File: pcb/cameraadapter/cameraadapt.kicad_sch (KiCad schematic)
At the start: 53 parts, among them J1 Conn_01x30_MountingPin, J2 Conn_01x24_MountingPin, J3 Conn_02x15_Odd_Even_MountingP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, J4 Conn_02x15_Odd_Even_MountingP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, J5 Conn_01x22_MountingPin, J6 Conn_01x22_MountingPin, Q1 DMG1024UV, U1 AP3429K, U3 ADP123, U4 ADP123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

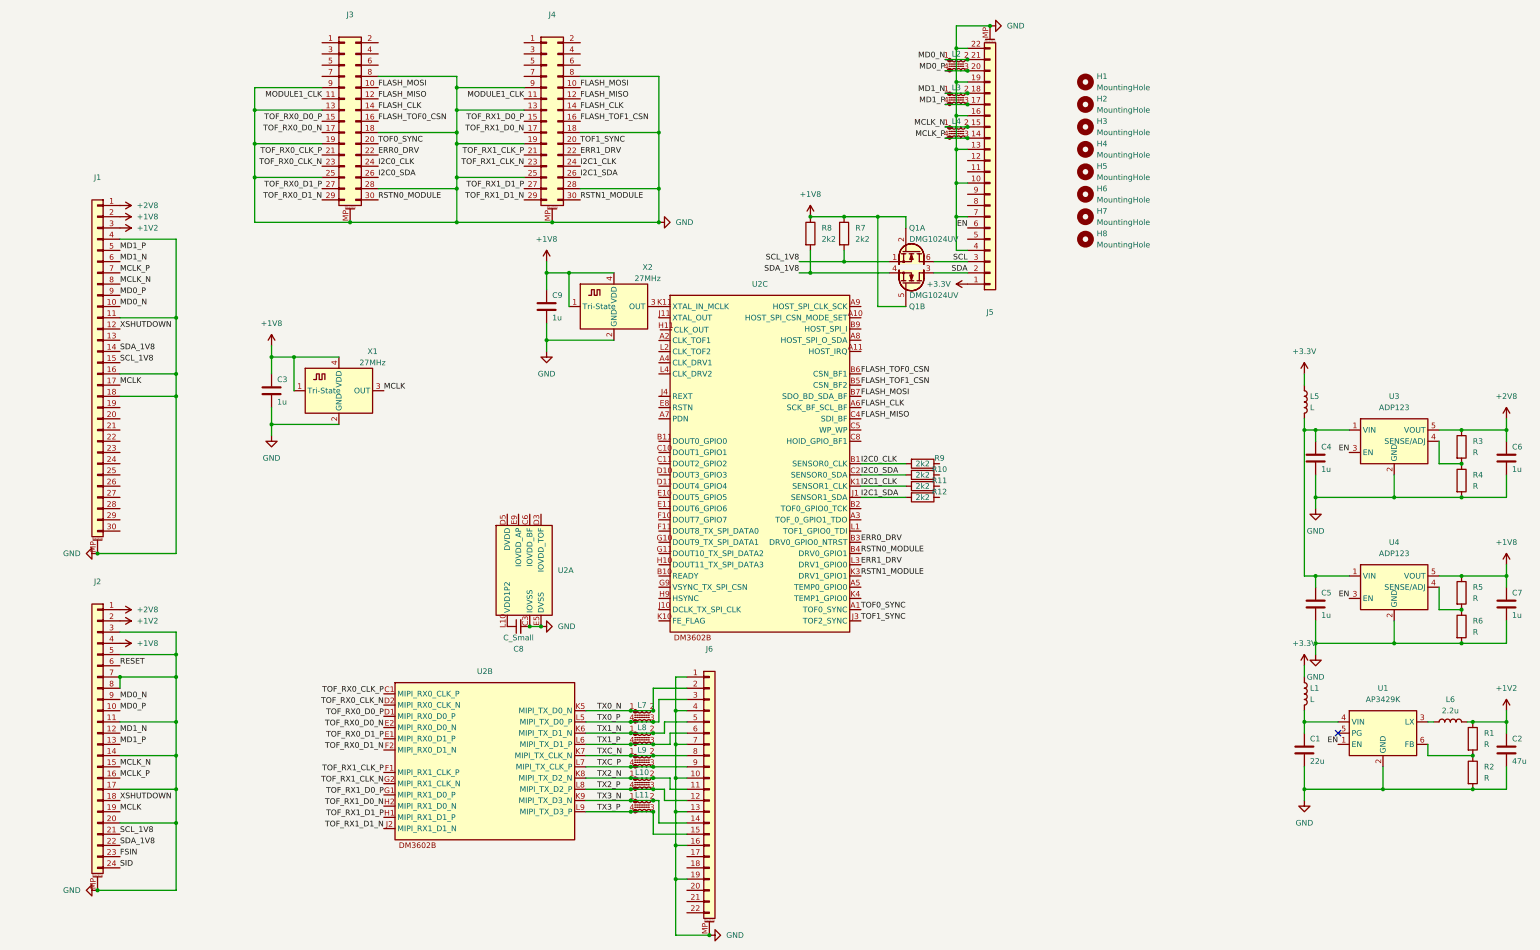
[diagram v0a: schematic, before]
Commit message: placement verification
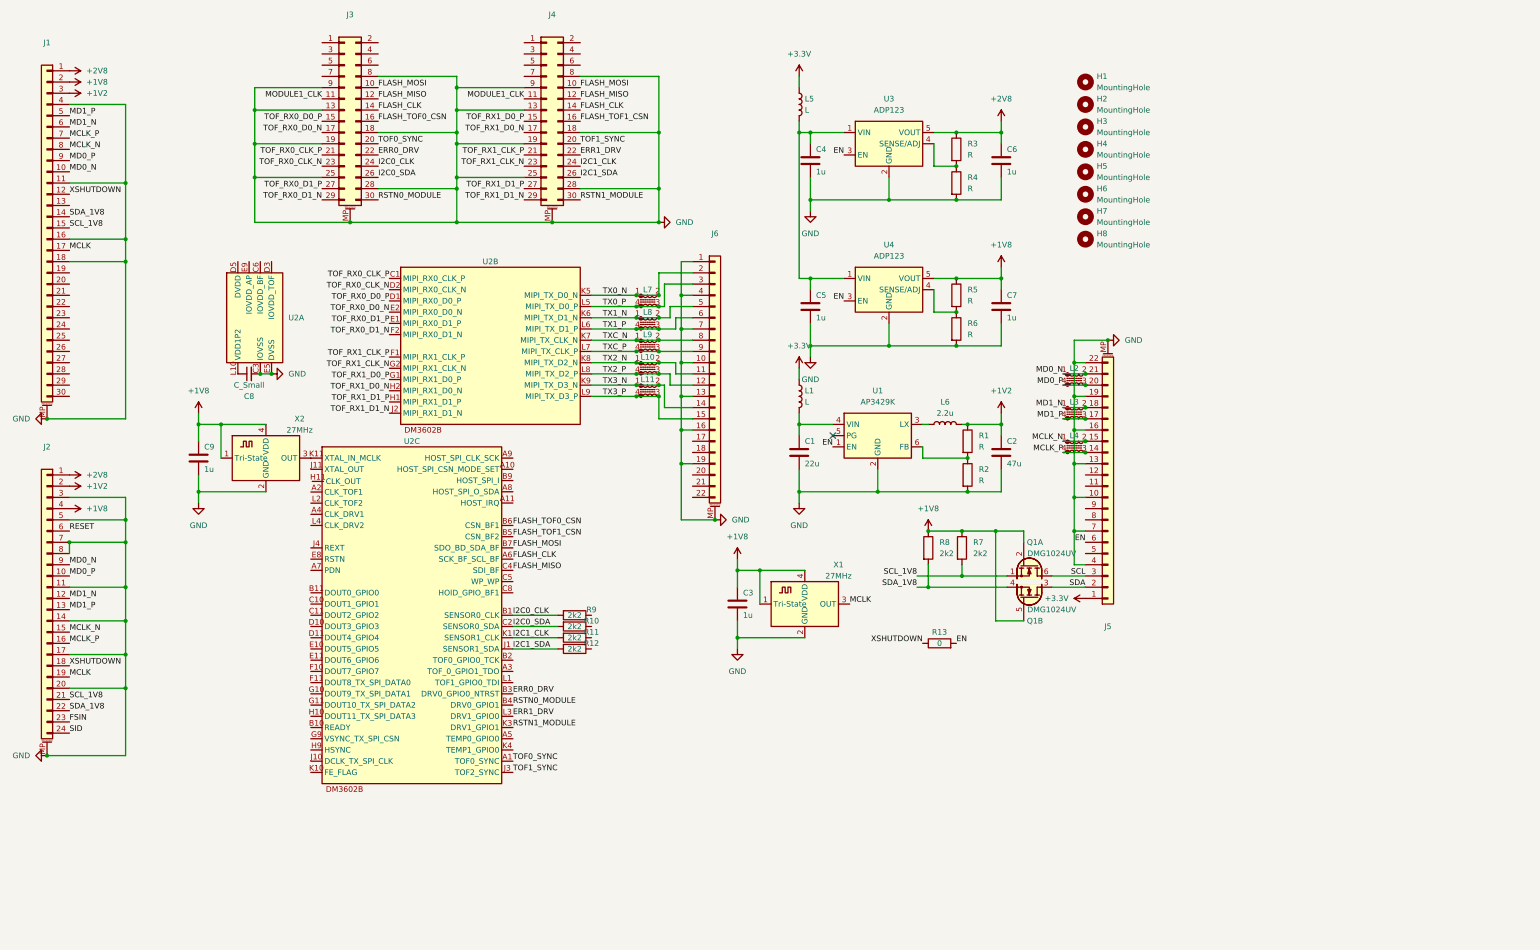
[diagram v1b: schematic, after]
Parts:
- added R13: 0, Resistor_SMD:R_0402_1005Metric, symbol Device:R
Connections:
- net EN: now also R13.2
- net XSHUTDOWN: now also R13.1
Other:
- moved on the sheet: C1, C2, C3, C4, C5, C6, C7, C8, C9, J1, J2, J5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
